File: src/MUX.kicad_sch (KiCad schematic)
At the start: 14 parts, among them U10 TMUX1208RSVR, U5 PCF8574RGTR(UMW), U6 PCF8574RGTR(UMW), U7 TMUX1208RSVR, U8 TMUX1208RSVR, U9 TMUX1208RSVR

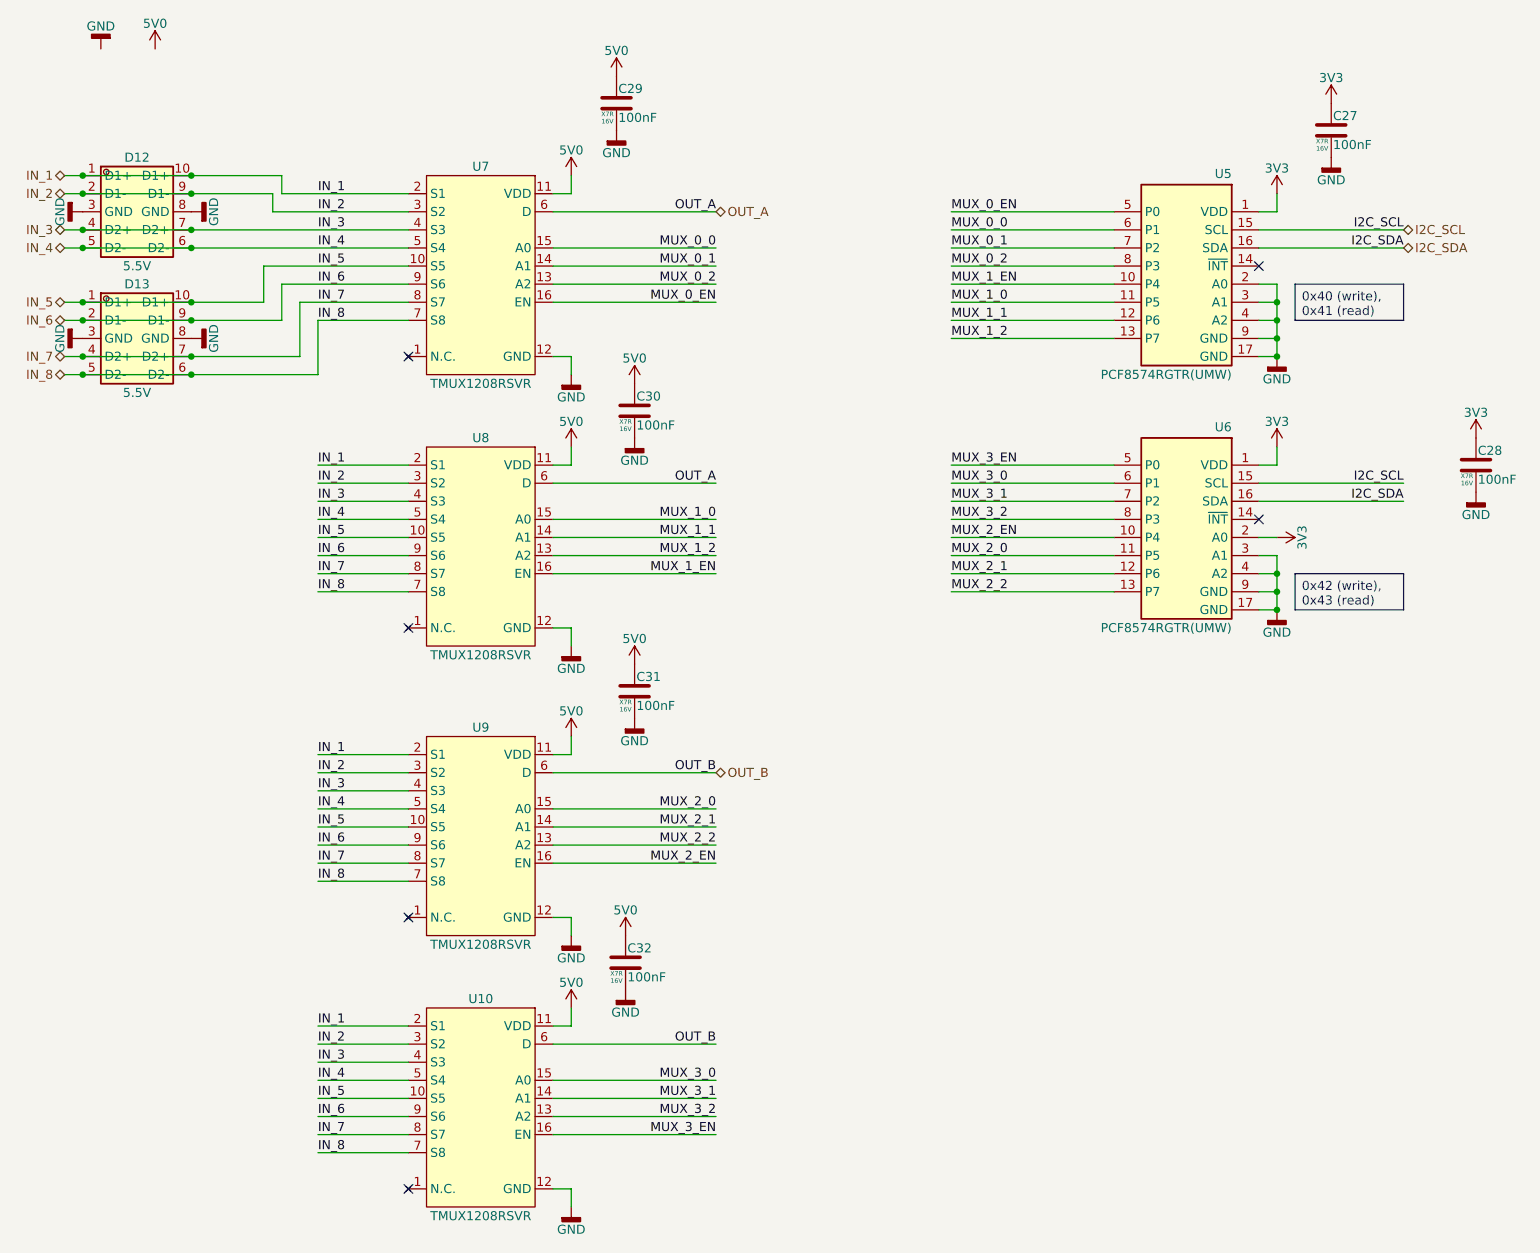
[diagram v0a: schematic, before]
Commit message: layout + lib swap to http library. changed up the 10u and 47u caps for cheaper alternative
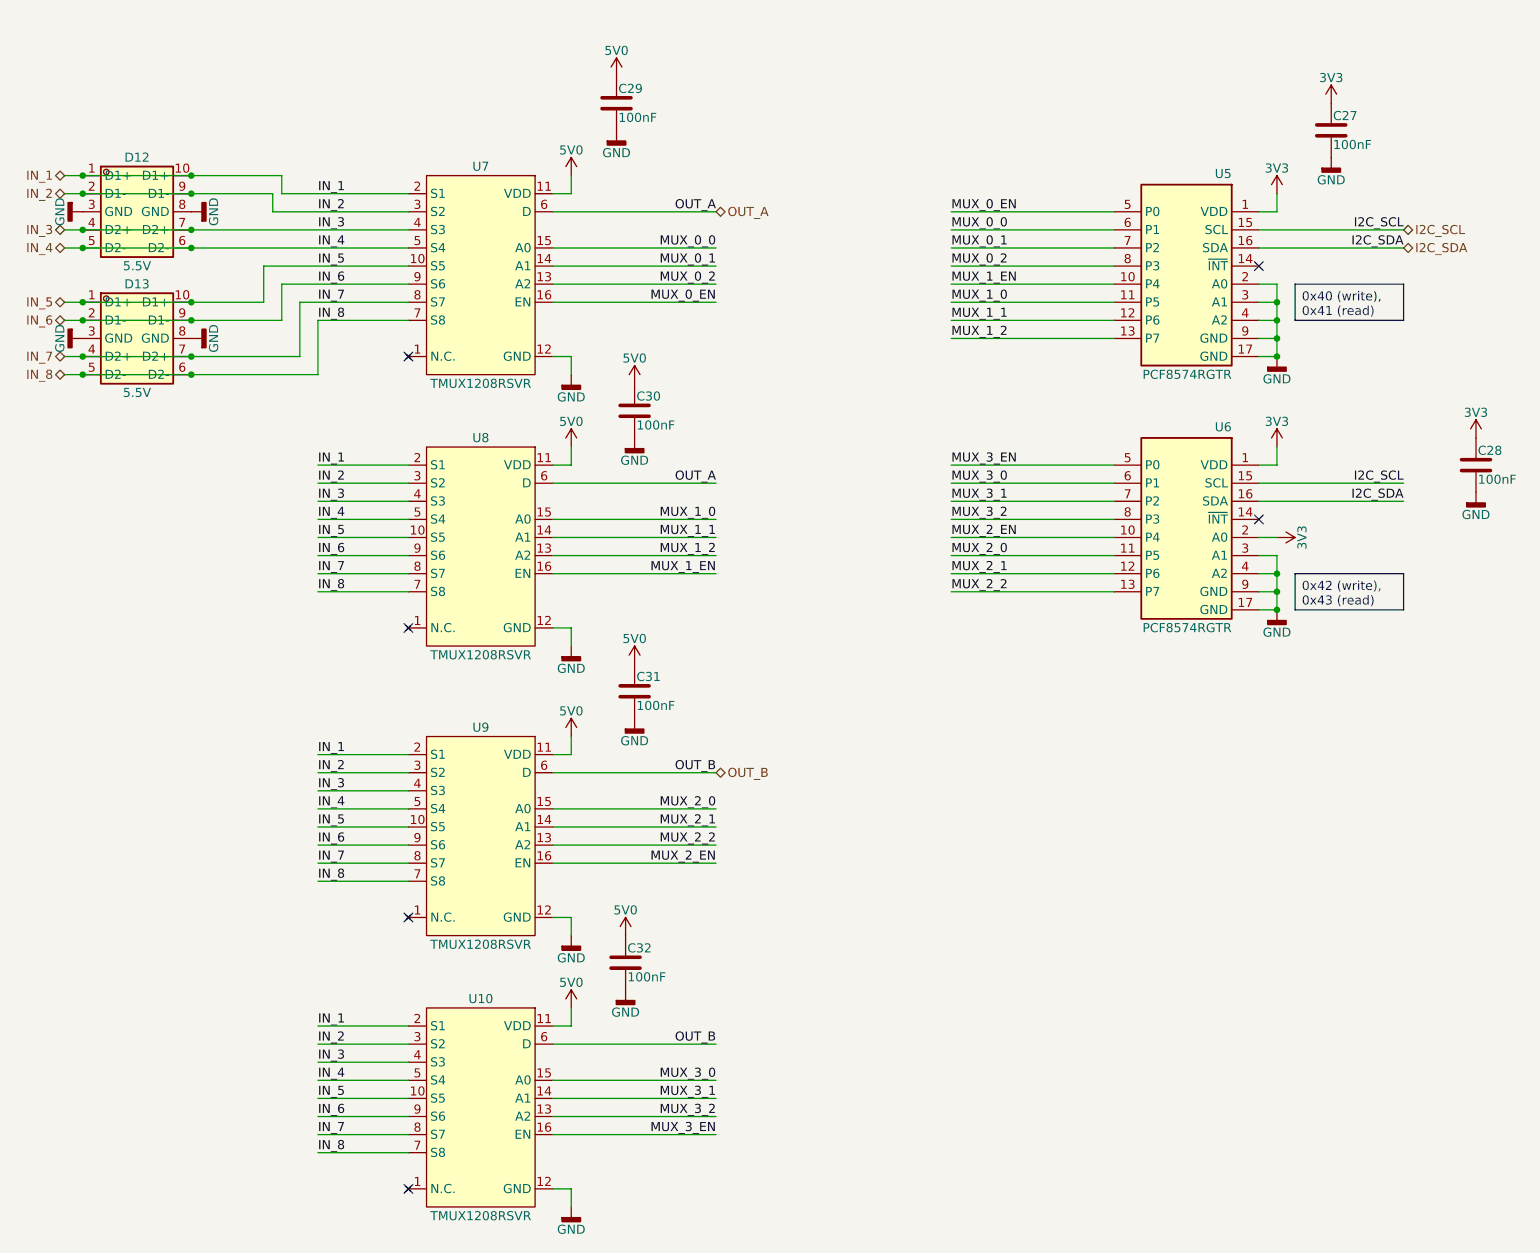
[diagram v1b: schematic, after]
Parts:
- C27, C28, C29, C30, C31, C32: footprint 7Sigma:C_0402_1005Metric -> PCM_7Sigma:C_0402_1005Metric; symbol Capacitor:CL05B104KO5NNNC -> 7Sigma:CL05B104KO5NNNC; Price @1 USD 0.0015 -> (none); Price @100 USD 0.0015 -> (none); Price @Bulk USD 0.0012 -> (none); Price Bulk Qty 1000 -> (none); Price Source LCSC -> (none); Price Updated 2026-05-14 -> (none)
- D12, D13: footprint 7Sigma:USON-10_2.5x1.0mm_P0.5mm -> PCM_7Sigma:USON-10_2.5x1.0mm_P0.5mm; symbol Diodes:TPD4E05U06DQAR -> 7Sigma:TPD4E05U06DQAR; Footprint_Name (none) -> USON-10; Manufacturer Part Number 1 TPD4E05U06DQAR -> (none); Price @1 USD 0.0875 -> (none); Price @100 USD 0.0717 -> (none); Price @Bulk USD 0.0570 -> (none); Price Bulk Qty 500 -> (none); Price Source LCSC -> (none); Price Updated 2026-07-19 -> (none)
- U10, U7, U8, U9: footprint 7Sigma:UQFN-16_1.8x2.6mm_P0.4mm -> PCM_7Sigma:UQFN-16_1.8x2.6mm_P0.4mm; symbol ICs:TMUX1208RSVR -> 7Sigma:TMUX1208RSVR; Channels (none) -> 8:1; Footprint_Name (none) -> UQFN-16; Price @1 USD 0.5658 -> (none); Price @100 USD 0.3486 -> (none); Price @Bulk USD 0.2999 -> (none); Price Bulk Qty 1000 -> (none); Price Source LCSC -> (none); Price Updated 2026-05-14 -> (none)
- U5, U6: value PCF8574RGTR(UMW) -> PCF8574RGTR; footprint 7Sigma:QFN-16-1EP_3x3mm_P0.5mm_EP1.7x1.7mm_ThermalVias -> PCM_7Sigma:QFN-16-1EP_3x3mm_P0.5mm_EP1.7x1.7mm_ThermalVias; symbol ICs:PCF8574RGTR -> 7Sigma:PCF8574RGTR; Manufacturer 1 UMW -> UMW (Youtai Semiconductor Co., Ltd.); Manufacturer Part Number 1 PCF8574RGTR(UMW) -> PCF8574RGTR; Price @1 USD 0.5030 -> (none); Price @100 USD 0.2854 -> (none); Price @Bulk USD 0.2419 -> (none); Price Bulk Qty 1000 -> (none); Price Source LCSC -> (none); Price Updated 2026-05-14 -> (none)
